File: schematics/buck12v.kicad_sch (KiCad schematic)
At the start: 11 parts

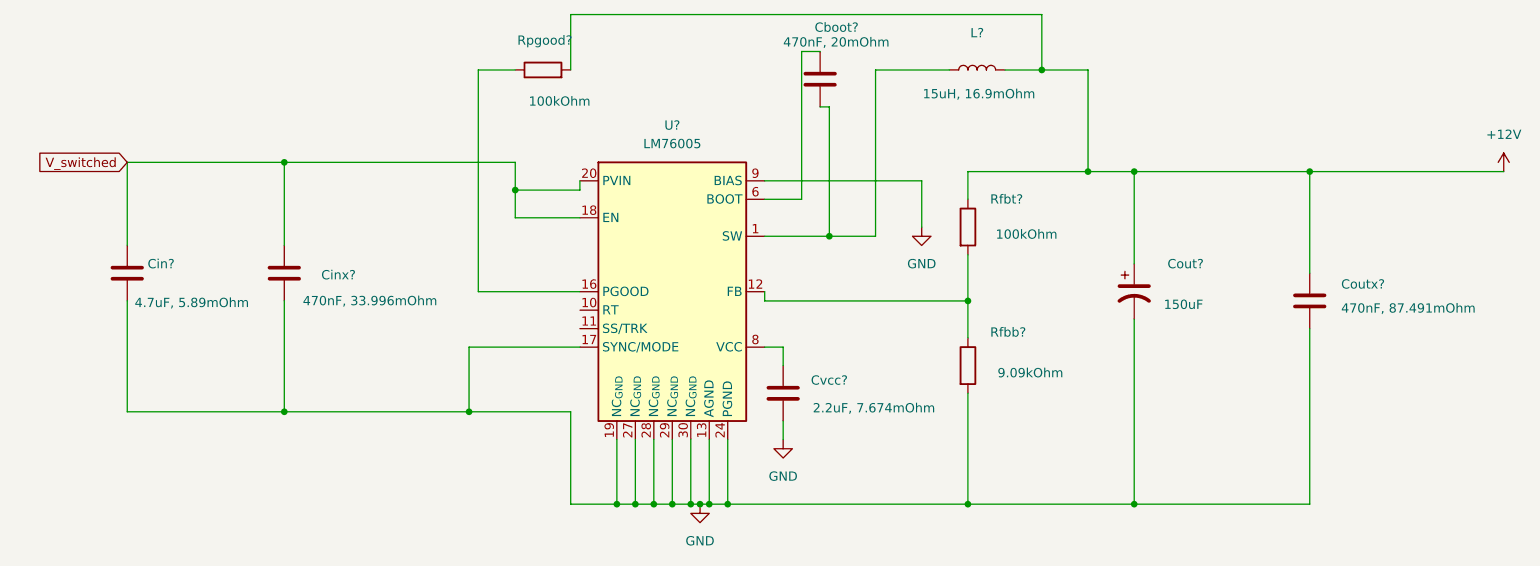
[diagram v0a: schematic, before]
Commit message: fixed footprints
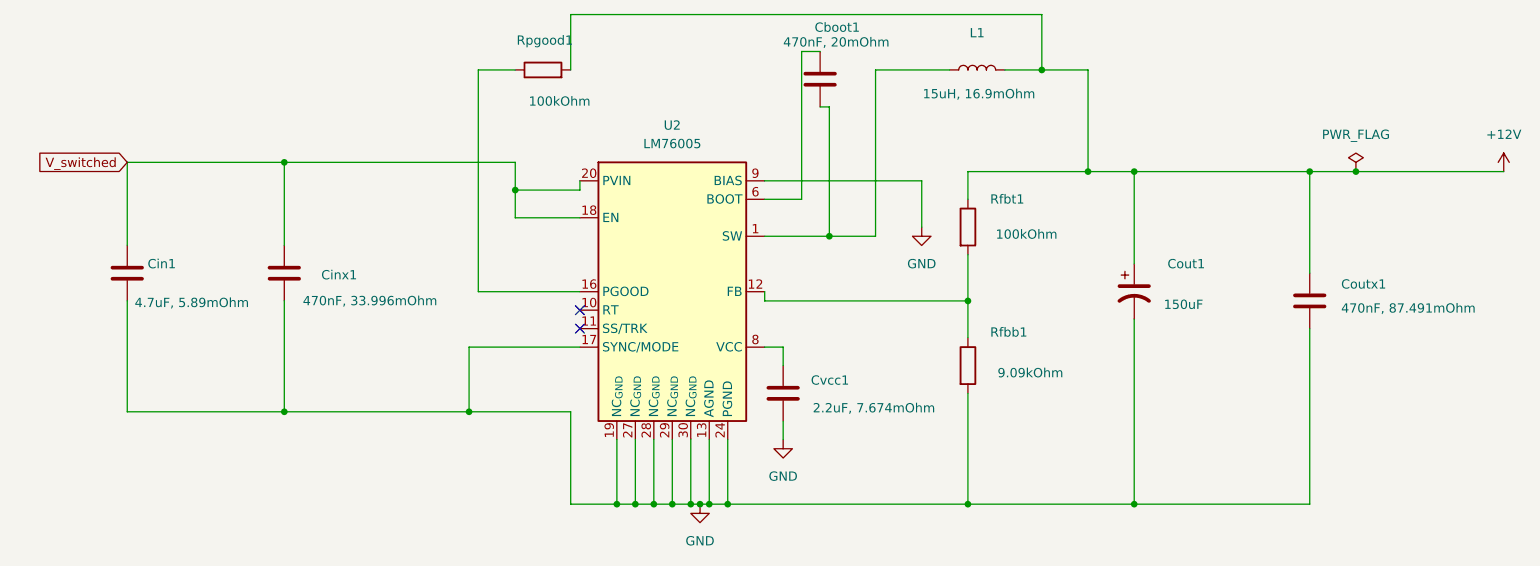
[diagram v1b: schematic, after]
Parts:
- gave numbers to parts that had none: 11
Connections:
- no-connect marks 0 -> 2
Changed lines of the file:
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@@
+	)
+	(junction
+		(at 240.03 80.01)
+		(diameter 0)
+		(color 0 0 0 0)
 	)
 	(junction
@@
 		(color 0 0 0 0)
 	)
+	(no_connect
+		(at 133.35 101.6)
+	)
+	(no_connect
+		(at 133.35 99.06)
+	)
 	(wire
 		(pts
@@
 	(wire
 		(pts
+			(xy 240.03 80.01) (xy 260.35 80.01)
+		)
+		(stroke
+			(width 0)
+			(type default)
+		)
+	)
+	(wire
+		(pts
 			(xy 92.71 97.79) (xy 92.71 113.03)
 		)
@@
 	(wire
 		(pts
-			(xy 233.68 80.01) (xy 260.35 80.01)
+			(xy 233.68 80.01) (xy 240.03 80.01)
 		)
 		(stroke
@@
 		(on_board yes)
 		(dnp no)
-		(property "Reference" "Coutx?"
+		(property "Reference" "Coutx1"
 			(at 237.998 95.504 0)
 			(effects
@@
 		(instances
 			(project "doggie_board"
-				(path "/883cb7fa-3eb5-48d4-9cde-7c11307d94f0/4477bd81-3edf-4db0-9be9-c00964857c14"
-					(reference "Coutx?")
-					(unit 1)
-				)
 				(path "/883cb7fa-3eb5-48d4-9cde-7c11307d94f0/ccf07133-5d0c-4081-9a30-ebff06623cf2"
 					(reference "Coutx1")
@@
 		(on_board yes)
 		(dnp no)
-		(property "Reference" "Cboot?"
+		(property "Reference" "Cboot1"
 			(at 165.608 60.198 0)
 			(effects
@@
 		(instances
 			(project "doggie_board"
-				(path "/883cb7fa-3eb5-48d4-9cde-7c11307d94f0/4477bd81-3edf-4db0-9be9-c00964857c14"
-					(reference "Cboot?")
-					(unit 1)
-				)
 				(path "/883cb7fa-3eb5-48d4-9cde-7c11307d94f0/ccf07133-5d0c-4081-9a30-ebff06623cf2"
 					(reference "Cboot1")
@@
 		(on_board yes)
 		(dnp no)
-		(property "Reference" "Cvcc?"
+		(property "Reference" "Cvcc1"
 			(at 165.1 108.712 0)
 			(effects
@@
 		(instances
 			(project "doggie_board"
-				(path "/883cb7fa-3eb5-48d4-9cde-7c11307d94f0/4477bd81-3edf-4db0-9be9-c00964857c14"
-					(reference "Cvcc?")
-					(unit 1)
-				)
 				(path "/883cb7fa-3eb5-48d4-9cde-7c11307d94f0/ccf07133-5d0c-4081-9a30-ebff06623cf2"
 					(reference "Cvcc1")
@@
 		(on_board yes)
 		(dnp no)
-		(property "Reference" "Rpgood?"
+		(property "Reference" "Rpgood1"
 			(at 128.524 61.976 90)
 			(effects
@@
 		(instances
 			(project "doggie_board"
-				(path "/883cb7fa-3eb5-48d4-9cde-7c11307d94f0/4477bd81-3edf-4db0-9be9-c00964857c14"
-					(reference "Rpgood?")
-					(unit 1)
-				)
 				(path "/883cb7fa-3eb5-48d4-9cde-7c11307d94f0/ccf07133-5d0c-4081-9a30-ebff06623cf2"
 					(reference "Rpgood1")
@@
 		(on_board yes)
 		(dnp no)
-		(property "Reference" "Cinx?"
+		(property "Reference" "Cinx1"
 			(at 97.79 94.234 0)
 			(effects
@@
 		(instances
 			(project "doggie_board"
-				(path "/883cb7fa-3eb5-48d4-9cde-7c11307d94f0/4477bd81-3edf-4db0-9be9-c00964857c14"
-					(reference "Cinx?")
-					(unit 1)
-				)
 				(path "/883cb7fa-3eb5-48d4-9cde-7c11307d94f0/ccf07133-5d0c-4081-9a30-ebff06623cf2"
 					(reference "Cinx1")
@@
 		(dnp no)
 		(fields_autoplaced yes)
-		(property "Reference" "#PWR?"
+		(property "Reference" "#PWR011"
 			(at 180.34 93.98 0)
 			(effects
@@
 		(instances
 			(project "doggie_board"
-				(path "/883cb7fa-3eb5-48d4-9cde-7c11307d94f0/4477bd81-3edf-4db0-9be9-c00964857c14"
-					(reference "#PWR?")
-					(unit 1)
-				)
 				(path "/883cb7fa-3eb5-48d4-9cde-7c11307d94f0/ccf07133-5d0c-4081-9a30-ebff06623cf2"
 					(reference "#PWR011")
@@
 		(on_board yes)
 		(dnp no)
-		(property "Reference" "Rfbt?"
+		(property "Reference" "Rfbt1"
 			(at 189.738 83.82 0)
 			(effects
@@
 		(instances
 			(project "doggie_board"
-				(path "/883cb7fa-3eb5-48d4-9cde-7c11307d94f0/4477bd81-3edf-4db0-9be9-c00964857c14"
-					(reference "Rfbt?")
-					(unit 1)
-				)
 				(path "/883cb7fa-3eb5-48d4-9cde-7c11307d94f0/ccf07133-5d0c-4081-9a30-ebff06623cf2"
 					(reference "Rfbt1")
@@
 		(on_board yes)
 		(dnp no)
-		(property "Reference" "Cout?"
+		(property "Reference" "Cout1"
 			(at 214.122 92.71 0)
 			(effects
@@
 		(instances
 			(project "doggie_board"
-				(path "/883cb7fa-3eb5-48d4-9cde-7c11307d94f0/4477bd81-3edf-4db0-9be9-c00964857c14"
-					(reference "Cout?")
-					(unit 1)
-				)
 				(path "/883cb7fa-3eb5-48d4-9cde-7c11307d94f0/ccf07133-5d0c-4081-9a30-ebff06623cf2"
 					(reference "Cout1")
@@
 		(dnp no)
 		(fields_autoplaced yes)
-		(property "Reference" "#PWR?"
+		(property "Reference" "#PWR013"
 			(at 161.29 123.19 0)
 			(effects
@@
 		(instances
 			(project "doggie_board"
-				(path "/883cb7fa-3eb5-48d4-9cde-7c11307d94f0/4477bd81-3edf-4db0-9be9-c00964857c14"
-					(reference "#PWR?")
-					(unit 1)
-				)
 				(path "/883cb7fa-3eb5-48d4-9cde-7c11307d94f0/ccf07133-5d0c-4081-9a30-ebff06623cf2"
 					(reference "#PWR013")
@@
 		(on_board yes)
 		(dnp no)
-		(property "Reference" "Rfbb?"
+		(property "Reference" "Rfbb1"
 			(at 189.738 102.108 0)
 			(effects
@@
 		(instances
 			(project "doggie_board"
-				(path "/883cb7fa-3eb5-48d4-9cde-7c11307d94f0/4477bd81-3edf-4db0-9be9-c00964857c14"
-					(reference "Rfbb?")
-					(unit 1)
-				)
 				(path "/883cb7fa-3eb5-48d4-9cde-7c11307d94f0/ccf07133-5d0c-4081-9a30-ebff06623cf2"
 					(reference "Rfbb1")
@@
 		(dnp no)
 		(fields_autoplaced yes)
-		(property "Reference" "U?"
+		(property "Reference" "U2"
 			(at 146.05 73.66 0)
 			(effects
@@
 		(instances
 			(project "doggie_board"
-				(path "/883cb7fa-3eb5-48d4-9cde-7c11307d94f0/4477bd81-3edf-4db0-9be9-c00964857c14"
-					(reference "U?")
-					(unit 1)
-				)
 				(path "/883cb7fa-3eb5-48d4-9cde-7c11307d94f0/ccf07133-5d0c-4081-9a30-ebff06623cf2"
 					(reference "U2")
@@
 		(dnp no)
 		(fields_autoplaced yes)
-		(property "Reference" "#PWR?"
+		(property "Reference" "#PWR07"
 			(at 260.35 83.82 0)
 			(effects
@@
 		(instances
 			(project "doggie_board"
-				(path "/883cb7fa-3eb5-48d4-9cde-7c11307d94f0/4477bd81-3edf-4db0-9be9-c00964857c14"
-					(reference "#PWR?")
-					(unit 1)
-				)
 				(path "/883cb7fa-3eb5-48d4-9cde-7c11307d94f0/ccf07133-5d0c-4081-9a30-ebff06623cf2"
 					(reference "#PWR07")
@@
 		(on_board yes)
 		(dnp no)
-		(property "Reference" "Cin?"
+		(property "Reference" "Cin1"
 			(at 73.914 92.71 0)
 			(effects
@@
 		(instances
 			(project "doggie_board"
-				(path "/883cb7fa-3eb5-48d4-9cde-7c11307d94f0/4477bd81-3edf-4db0-9be9-c00964857c14"
-					(reference "Cin?")
-					(unit 1)
-				)
 				(path "/883cb7fa-3eb5-48d4-9cde-7c11307d94f0/ccf07133-5d0c-4081-9a30-ebff06623cf2"
 					(reference "Cin1")
+					(unit 1)
+				)
+			)
+		)
+	)
+	(symbol
+		(lib_id "power:PWR_FLAG")
+		(at 240.03 80.01 0)
+		(unit 1)
+		(exclude_from_sim no)
+		(in_bom yes)
+		(on_board yes)
+		(dnp no)
+		(fields_autoplaced yes)
+		(property "Reference" "#FLG03"
+			(at 240.03 78.105 0)
+			(effects
+				(font
+					(size 1.27 1.27)
+				)
+				(hide yes)
+			)
+		)
+		(property "Value" "PWR_FLAG"
+			(at 240.03 74.93 0)
+			(effects
+				(font
+					(size 1.27 1.27)
+				)
+			)
+		)
+		(property "Footprint" ""
+			(at 240.03 80.01 0)
+			(effects
+				(font
+					(size 1.27 1.27)
+				)
+				(hide yes)
+			)
+		)
+		(property "Datasheet" "~"
+			(at 240.03 80.01 0)
+			(effects
+				(font
+					(size 1.27 1.27)
+				)
+				(hide yes)
+			)
+		)
+		(property "Description" "Special symbol for telling ERC where power comes from"
+			(at 240.03 80.01 0)
+			(effects
+				(font
+					(size 1.27 1.27)
+				)
+				(hide yes)
+			)
+		)
+		(pin "1"
+		)
+		(instances
+			(project ""
+				(path "/883cb7fa-3eb5-48d4-9cde-7c11307d94f0/ccf07133-5d0c-4081-9a30-ebff06623cf2"
+					(reference "#FLG03")
 					(unit 1)
 				)
@@
 		(dnp no)
 		(fields_autoplaced yes)
-		(property "Reference" "#PWR?"
+		(property "Reference" "#PWR014"
 			(at 149.86 132.08 0)
 			(effects
@@
 		(instances
 			(project "doggie_board"
-				(path "/883cb7fa-3eb5-48d4-9cde-7c11307d94f0/4477bd81-3edf-4db0-9be9-c00964857c14"
-					(reference "#PWR?")
-					(unit 1)
-				)
 				(path "/883cb7fa-3eb5-48d4-9cde-7c11307d94f0/ccf07133-5d0c-4081-9a30-ebff06623cf2"
 					(reference "#PWR014")
@@
 		(on_board yes)
 		(dnp no)
-		(property "Reference" "L?"
+		(property "Reference" "L1"
 			(at 187.96 60.96 90)
 			(effects
@@
 		(instances
 			(project "doggie_board"
-				(path "/883cb7fa-3eb5-48d4-9cde-7c11307d94f0/4477bd81-3edf-4db0-9be9-c00964857c14"
-					(reference "L?")
-					(unit 1)
-				)
 				(path "/883cb7fa-3eb5-48d4-9cde-7c11307d94f0/ccf07133-5d0c-4081-9a30-ebff06623cf2"
 					(reference "L1")
